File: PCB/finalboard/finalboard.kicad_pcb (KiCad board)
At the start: 4 copper layers, 109.2 x 73.7 mm, 33 parts, among them J1 USB_C_Receptacle_USB2.0, J2 Conn_01x02, J3 Conn_01x04, J6 AudioJack4, Q1 MMDT3904, U1 ESP32-S3-WROOM-1, U3 USBLC6-2SC6, U5 SN74LVC1T45DRL, U6 SN74LVC1T45DRL, U7 AMS1117-3.3, U8 MCP73831-2-OT

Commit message: Incorporated Feedback
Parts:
- removed ?: , 
- removed TP2: TestPoint, TestPoint:TestPoint_Pad_D4.0mm
- added C4: 10u, Capacitor_SMD:C_1206_3216Metric, F.Cu at (82.3, 46.0)
- added C5: 10u, Capacitor_SMD:C_1206_3216Metric, F.Cu at (138.2, 49.5)
- added C6: 0.1u, Capacitor_SMD:C_1206_3216Metric, F.Cu at (92.2, 44.7)
- added D4: GREEN, LED_SMD:LED_1206_3216Metric, B.Cu at (60.7, 32.3)
- added D5: YELLOW, LED_SMD:LED_1206_3216Metric, B.Cu at (85.3, 99.6)
- added D6: 1N5822, Diode_THT:D_DO-201AD_P15.24mm_Horizontal, F.Cu at (89.8, 114.9)
- added D7: BLUE, LED_SMD:LED_1206_3216Metric, F.Cu at (74.7, 111.8)
- added J4: Conn_01x04, Connector_PinHeader_2.54mm:PinHeader_1x04_P2.54mm_Vertical, F.Cu at (32.8, 104.9)
- added J5: Conn_01x02, Connector_PinHeader_2.54mm:PinHeader_1x02_P2.54mm_Vertical, F.Cu at (55.4, 110.9)
- added J7: Conn_01x04, Connector_PinHeader_2.54mm:PinHeader_1x04_P2.54mm_Vertical, F.Cu at (43.9, 106.2)
- added Q3: S8550, Package_TO_SOT_THT:TO-92_Inline, F.Cu at (82.3, 40.1)
- added R10: 10k, Resistor_SMD:R_1206_3216Metric, F.Cu at (125.5, 51.1)
- added R11: 10k, Resistor_SMD:R_1206_3216Metric, F.Cu at (125.5, 54.3)
- added R12: 10k, Resistor_SMD:R_1206_3216Metric, F.Cu at (90.2, 120.0)
- added R13: 100k, Resistor_SMD:R_1206_3216Metric, F.Cu at (90.2, 123.2)
- added R14: R, Resistor_SMD:R_1206_3216Metric, F.Cu at (74.6, 115.2)
- added R15: 6.8k, Resistor_SMD:R_1206_3216Metric, F.Cu at (60.5, 110.2)
- added R16: 10k, Resistor_SMD:R_1206_3216Metric, F.Cu at (60.5, 113.5)
- added R17: 100k, Resistor_SMD:R_1206_3216Metric, F.Cu at (91.9, 49.5)
- added R6: 220, Resistor_SMD:R_1206_3216Metric, F.Cu at (90.4, 40.1)
- added R7: 1000, Resistor_SMD:R_1206_3216Metric, F.Cu at (75.9, 40.9)
- added R8: 4.7k, Resistor_SMD:R_1206_3216Metric, F.Cu at (130.8, 84.8)
- added R9: 470, Resistor_SMD:R_1206_3216Metric, F.Cu at (85.3, 95.2)
- added U10: SN74LVC1T45DRL, Package_TO_SOT_SMD:SOT-563, F.Cu at (121.7, 90.9)
- added U11: MCP23008-xSO, Package_SO:SOIC-18W_7.5x11.6mm_P1.27mm, F.Cu at (80.8, 82.3)
- added U9: SN74LVC1T45DRL, Package_TO_SOT_SMD:SOT-563, F.Cu at (121.7, 87.6)
- D1: value LED -> RED
- D2: value LED -> BLUE
- D3: value LED -> YELLOW
- Q1: value MMDT3904 -> DMG2301L; footprint Package_TO_SOT_SMD:SOT-363_SC-70-6 -> Package_TO_SOT_SMD:SOT-23
- R3, R4, R5: value R -> 470
- moved R5 57.5 mm to (125.2, 42.7)
- moved R3 43.0 mm to (95.2, 53.3)
- moved R4 38.7 mm to (95.2, 56.6)
- moved D3 34.3 mm to (95.2, 32.8)
- moved U8 25.0 mm to (131.1, 89.9)
- moved U7 3.96 mm to (114.0, 82.0)
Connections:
- net Net-(U5-B) renamed /CA_RX
- net Net-(U5-VCCB) renamed /CA_5V
- net Net-(U6-B) renamed /CA_TX
- C1 pad 1: Net-(U3-VBUS) -> Net-(U7-VI)
- D1 pad 1: Net-(D1-K) -> GND
- D1 pad 2: Net-(D1-A) -> /RECORDING_LED
- D2 pad 1: Net-(D2-K) -> GND
- D2 pad 2: Net-(D2-A) -> /WIFI_LED
- D3 pad 1: Net-(D3-K) -> GND
- D3 pad 2: Net-(D3-A) -> /SDCARD_LED
- J1 pad A4: Net-(U3-VBUS) -> /VBUS
- J1 pad A9: Net-(U3-VBUS) -> /VBUS
- J1 pad B4: Net-(U3-VBUS) -> /VBUS
- J1 pad B9: Net-(U3-VBUS) -> /VBUS
- J2 pad 1: unconnected-(J2-Pin_1-Pad1) -> /VBAT
- J2 pad 2: unconnected-(J2-Pin_2-Pad2) -> GND
- J3 pad 1: unconnected-(J3-Pin_1-Pad1) -> /BMS_RX
- J3 pad 2: /ESP_TX2 -> /BMS_TX
- J3 pad 3: /ESP_RX2 -> /BMS_VCC
- Q1 pad 1: Net-(Q1A-E1) -> /VBUS
- Q1 pad 2: /PWR_TRAN_LCD -> Net-(D6-K)
- Q1 pad 3: +3V3 -> /VBAT
- R3 pad 1: GND -> Net-(U4-RXD)
- R3 pad 2: Net-(D1-K) -> /ESP_SS_TX0
- R4 pad 1: GND -> Net-(U4-TX0)
- R4 pad 2: Net-(D2-K) -> /ESP_SS_RX0
- R5 pad 1: GND -> Net-(J4-Pin_2)
- R5 pad 2: Net-(D3-K) -> /ESP_TX0
- U1 pad 12: Net-(D1-A) -> /SDA
- U1 pad 17: Net-(D2-A) -> /SCL
- U1 pad 27: unconnected-(U1-GPIO0/BOOT-Pad27) -> Net-(J5-Pin_2)
- U1 pad 3: unconnected-(U1-EN-Pad3) -> Net-(U1-EN)
- U1 pad 31: Net-(D3-A) -> unconnected-(U1-GPIO38/FSPIWP/SUBSPIWP-Pad31)
- U1 pad 32: unconnected-(U1-MTCK/GPIO39/CLK_OUT3/SUBSPICS1-Pad32) -> Net-(J7-Pin_4)
- U1 pad 33: unconnected-(U1-MTDO/GPIO40/CLK_OUT2-Pad33) -> Net-(J7-Pin_3)
- U1 pad 34: unconnected-(U1-MTDI/GPIO41/CLK_OUT1-Pad34) -> Net-(J7-Pin_2)
- U1 pad 35: unconnected-(U1-MTMS/GPIO42-Pad35) -> Net-(J7-Pin_1)
- U1 pad 38: /PWR_TRAN_TFT -> /LCD_DC
- U1 pad 39: /PWR_TRAN_LCD -> /LED_BACKLIGHT
- U1 pad 4: Net-(U1-GPIO4/TOUCH4/ADC1_CH3) -> /ADC_Battery
- U2 pad 1: Net-(Q1B-E2) -> +3V3
- U2 pad 5: unconnected-(U2-DC/RS-Pad5) -> /LCD_DC
- U2 pad 8: Net-(Q1A-E1) -> /LED_BACKLIGHT
- U3 pad 5: Net-(U3-VBUS) -> /VBUS
- U4 pad 3: /ESP_SS_TX0 -> Net-(U4-RXD)
- U4 pad 4: /ESP_SS_RX0 -> Net-(U4-TX0)
- U4 pad 5: unconnected-(U4-PPS-Pad5) -> Net-(U4-PPS)
- U7 pad 3: Net-(U3-VBUS) -> Net-(U7-VI)
- U8 pad 1: unconnected-(U8-STAT-Pad1) -> Net-(D5-K)
- U8 pad 2: unconnected-(U8-V_{SS}-Pad2) -> GND
- U8 pad 3: unconnected-(U8-V_{BAT}-Pad3) -> /VBAT
- U8 pad 4: unconnected-(U8-V_{DD}-Pad4) -> /VBUS
- U8 pad 5: unconnected-(U8-PROG-Pad5) -> Net-(U8-PROG)
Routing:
- net Net-(J4-Pin_2): track 0.00 -> 18.0 mm, vias 0 -> 1
- net GND: track 22.8 -> 4.70 mm, vias 2 -> 1
- net Net-(D1-K): track 7.97 -> 0.00 mm, vias 1 -> 0
- net /ESP_SS_TX0: track 0.00 -> 7.97 mm
- net Net-(D2-K): track 6.70 -> 0.00 mm, vias 1 -> 0
- net /ADC_Battery: track 0.00 -> 6.70 mm, vias 0 -> 1
- net Net-(U1-EN): track 0.00 -> 5.43 mm, vias 0 -> 1
- net Net-(D3-K): track 5.43 -> 0.00 mm, vias 1 -> 0
- net /VBAT: vias 0 -> 1
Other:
- board text added: "Charging"
- board text added: "GPS"

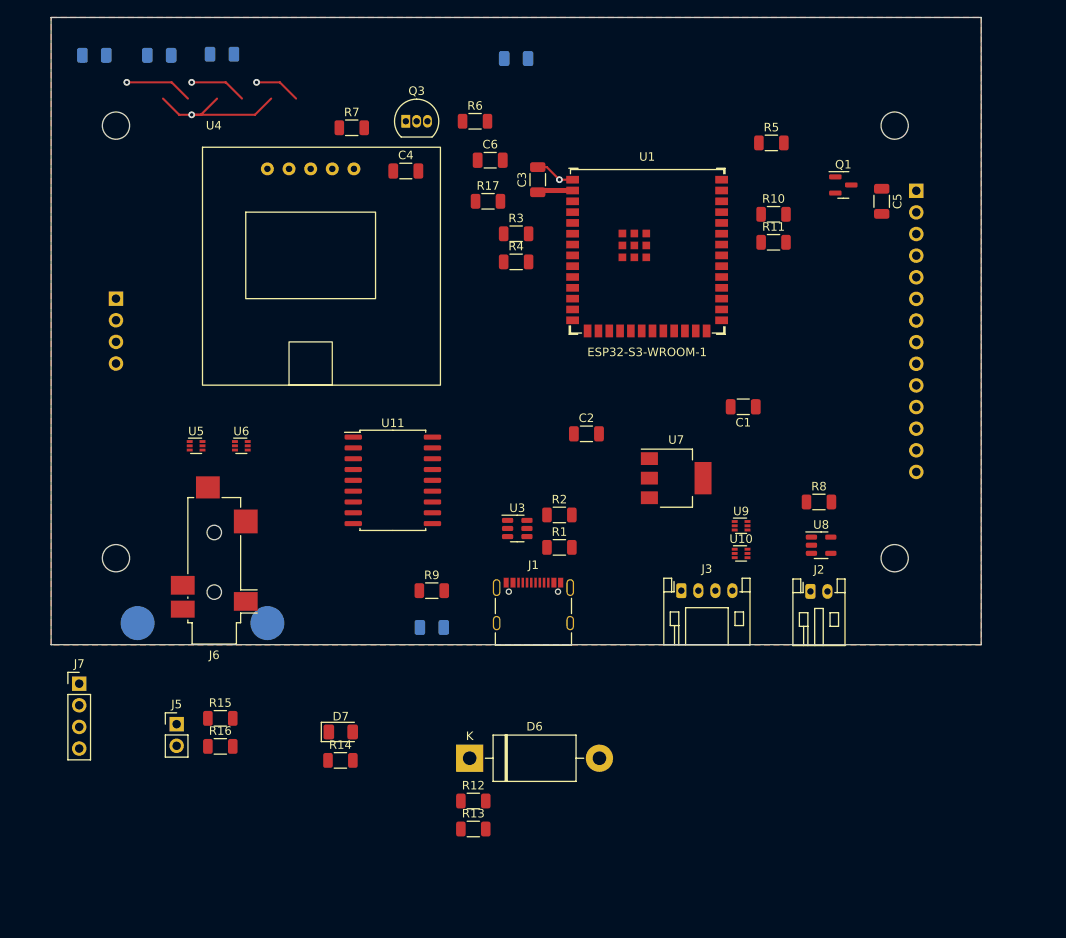
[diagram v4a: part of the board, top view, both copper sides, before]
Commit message: Schematic Mostly Done
check esp32 pins
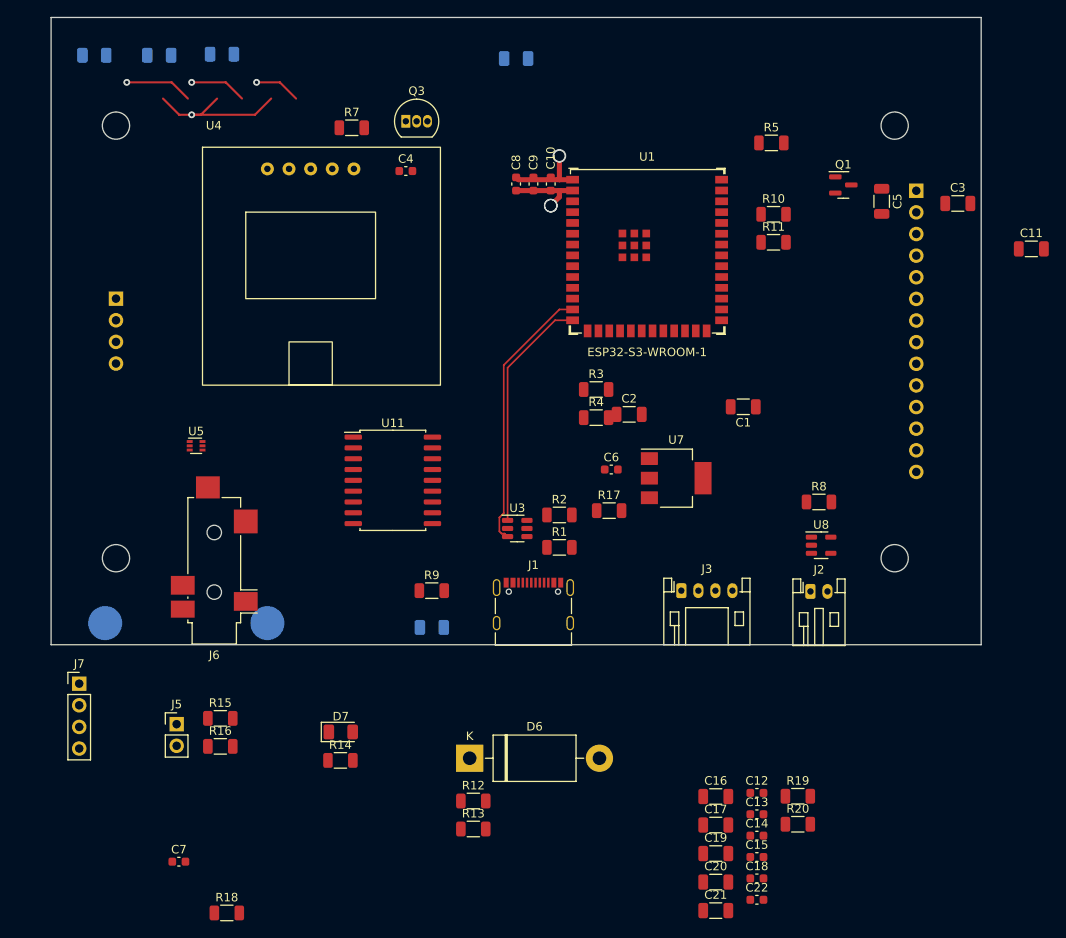
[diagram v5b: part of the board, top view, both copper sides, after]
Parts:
- removed R6: 220, Resistor_SMD:R_1206_3216Metric
- removed TP3: TestPoint, TestPoint:TestPoint_Pad_D4.0mm
- removed U10, U6, U9: SN74LVC1T45DRL, Package_TO_SOT_SMD:SOT-563
- added C10: 0.1u, Capacitor_SMD:C_0603_1608Metric, F.Cu at (99.3, 47.5)
- added C11: 1u, Capacitor_SMD:C_1206_3216Metric, F.Cu at (155.8, 55.1)
- added C12: 0.1u, Capacitor_SMD:C_0603_1608Metric, F.Cu at (123.5, 119.0)
- added C13: 0.1u, Capacitor_SMD:C_0603_1608Metric, F.Cu at (123.5, 121.5)
- added C14: 0.1u, Capacitor_SMD:C_0603_1608Metric, F.Cu at (123.5, 124.0)
- added C15: 0.1u, Capacitor_SMD:C_0603_1608Metric, F.Cu at (123.5, 126.5)
- added C16: 10u, Capacitor_SMD:C_1206_3216Metric, F.Cu at (118.7, 119.4)
- added C17: 10u, Capacitor_SMD:C_1206_3216Metric, F.Cu at (118.7, 122.8)
- added C18: 0.1u, Capacitor_SMD:C_0603_1608Metric, F.Cu at (123.5, 129.0)
- added C19: 0.1u, Capacitor_SMD:C_1206_3216Metric, F.Cu at (118.7, 126.1)
- added C20: 10u, Capacitor_SMD:C_1206_3216Metric, F.Cu at (118.7, 129.5)
- added C21: 10u, Capacitor_SMD:C_1206_3216Metric, F.Cu at (118.7, 132.8)
- added C22: 0.1u, Capacitor_SMD:C_0603_1608Metric, F.Cu at (123.5, 131.6)
- added C7: 1u, Capacitor_SMD:C_0603_1608Metric, F.Cu at (55.6, 127.1)
- added C8: 22u, Capacitor_SMD:C_0603_1608Metric, F.Cu at (95.2, 47.5)
- added C9: 1u, Capacitor_SMD:C_0603_1608Metric, F.Cu at (97.3, 47.5)
- added R18: 100, Resistor_SMD:R_1206_3216Metric, F.Cu at (61.3, 133.1)
- added R19: 470, Resistor_SMD:R_1206_3216Metric, F.Cu at (128.3, 119.4)
- added R20: 470, Resistor_SMD:R_1206_3216Metric, F.Cu at (128.3, 122.7)
- added TP2: TestPoint, TestPoint:TestPoint_Pad_D4.0mm, B.Cu at (47.0, 99.1)
- C1, C2, C5: value 10u -> 22u
- C4, C6: footprint Capacitor_SMD:C_1206_3216Metric -> Capacitor_SMD:C_0603_1608Metric
- R12: value 10k -> 470
- R14: value R -> 470
- R17: value 100k -> 10K
- moved C3 49.4 mm to (147.1, 49.8), turned to 0 degrees
- moved C6 39.0 mm to (106.4, 81.0)
- moved R17 39.0 mm to (106.2, 85.9)
- moved R4 20.6 mm to (104.6, 74.9)
- moved R3 20.6 mm to (104.6, 71.6)
- moved C2 5.51 mm to (108.5, 74.5)
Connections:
- net /SS1 renamed /CS_SD
- net Net-(J5-Pin_2) renamed /BOOT
- net Net-(U7-VI) renamed /Vinput
- D4 pad 2: Net-(D4-A) -> +3V3
- D7 pad 1: Net-(D7-K) -> GND
- J4 pad 4: +3V3 -> /VCC
- R10 pad 2: /SDA -> /SCL
- R11 pad 2: /SCL -> /SDA
- R12 pad 1: Net-(U1-EN) -> Net-(U12-A1)
- R12 pad 2: Net-(R12-Pad2) -> /ESP_TX1
- R14 pad 1: GND -> Net-(U12-A2)
- R14 pad 2: Net-(D7-K) -> /ESP_RX1
- R15 pad 1: /ADC_Battery -> /DIVIDED_VBAT
- R16 pad 2: /ADC_Battery -> /DIVIDED_VBAT
- TP1 pad 1: Net-(U1-GPIO3/TOUCH3/ADC1_CH2) -> Net-(U1-GPIO1/TOUCH1/ADC1_CH0)
- U1 pad 10: /ESP_RX1 -> /ESP_TX1
- U1 pad 11: /ESP_TX2 -> /ESP_RX1
- U1 pad 15: Net-(U1-GPIO3/TOUCH3/ADC1_CH2) -> /DIVIDED_VBAT
- U1 pad 22: /ESP_TX1 -> /CS_LCD
- U1 pad 23: /ESP_RX2 -> /CS_TOUCH
- U1 pad 24: unconnected-(U1-GPIO47/SPICLK_P/SUBSPICLK_P_DIFF-Pad24) -> /LCD_BACKLIGHT
- U1 pad 25: unconnected-(U1-GPIO48/SPICLK_N/SUBSPICLK_N_DIFF-Pad25) -> /LCD_DC
- U1 pad 31: unconnected-(U1-GPIO38/FSPIWP/SUBSPIWP-Pad31) -> /LED_BUILTIN
- U1 pad 38: /LCD_DC -> Net-(U1-GPIO2/TOUCH2/ADC1_CH1)
- U1 pad 39: /LED_BACKLIGHT -> Net-(U1-GPIO1/TOUCH1/ADC1_CH0)
- U1 pad 4: /ADC_Battery -> /ESP_TX2
- U1 pad 5: Net-(U1-GPIO5/TOUCH5/ADC1_CH4) -> /ESP_RX2
- U1 pad 8: unconnected-(U1-GPIO15/U0RTS/ADC2_CH4/XTAL_32K_P-Pad8) -> /LCD_TIRQ
- U2 pad 11: /SS3 -> /CS_TOUCH
- U2 pad 14: unconnected-(U2-T_IRQ-Pad14) -> /LCD_TIRQ
- U2 pad 3: /SS2 -> /CS_LCD
- U2 pad 8: /LED_BACKLIGHT -> /LCD_BACKLIGHT
- U8 pad 1: Net-(D5-K) -> Net-(U8-STAT)
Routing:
- net /USB_D-: track 0.00 -> 31.7 mm
- net /USB_D+: track 0.00 -> 27.9 mm
- net /VBAT: track 0.00 -> 7.97 mm
- net /ESP_SS_TX0: track 7.97 -> 0.00 mm
- net /ESP_TX2: track 0.00 -> 6.70 mm, vias 0 -> 1
- net /ADC_Battery: track 6.70 -> 0.00 mm, vias 1 -> 0
- net GND: track 4.70 -> 9.53 mm
- net +3V3: track 4.17 -> 8.82 mm, vias 0 -> 2
- added copper zone on In2.Cu, net +3V3
- removed copper zone on F.Cu, net +3V3

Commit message: Fixed Footprints, connected all nets
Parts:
- removed C20, C21: 10u, Capacitor_SMD:C_1206_3216Metric
- removed C22: 0.1u, Capacitor_SMD:C_0603_1608Metric
- removed Q3: S8550, Package_TO_SOT_THT:TO-92_Inline
- removed R13: 100k, Resistor_SMD:R_1206_3216Metric
- removed R14, R20: 470, Resistor_SMD:R_1206_3216Metric
- removed R15: 6.8k, Resistor_SMD:R_1206_3216Metric
- removed R16: 10k, Resistor_SMD:R_1206_3216Metric
- removed REF** (x4): MountingHole_3.2mm_M3, MountingHole:MountingHole_3.2mm_M3
- removed U11: MCP23008-xSO, Package_SO:SOIC-18W_7.5x11.6mm_P1.27mm
- added D8: GREEN, LED_SMD:LED_1206_3216Metric, B.Cu at (35.8, 43.4)
- added J8: Conn_01x04, Connector_JST:JST_PH_S4B-PH-K_1x04_P2.00mm_Horizontal, F.Cu at (98.5, 45.9)
- added Q2: S8550, Package_TO_SOT_SMD:SOT-23, F.Cu at (49.1, 50.0)
- added R6: 470, Resistor_SMD:R_1206_3216Metric, F.Cu at (105.7, 81.3)
- added SW1: SW_DIP_x01, Button_Switch_THT:SW_PUSH_6mm_H5mm, B.Cu at (81.8, 41.5)
- added SW2: SW_DIP_x01, Button_Switch_THT:Push_E-Switch_KS01Q01, F.Cu at (82.4, 133.2)
- added U6: PI4ULS5V202, wc_sys_footprint:PI4ULS5V202UEX, F.Cu at (101.8, 52.5)
- added U9: ~, wc_sys_footprint:GT-U7, F.Cu at (46.9, 77.2)
- C1: value 22u -> 0.1u; footprint Capacitor_SMD:C_1206_3216Metric -> Capacitor_SMD:C_0603_1608Metric
- C10, C12, C13: value 0.1u -> 10u; footprint Capacitor_SMD:C_0603_1608Metric -> Capacitor_SMD:C_1206_3216Metric
- C11: value 1u -> 0.1u; footprint Capacitor_SMD:C_1206_3216Metric -> Capacitor_SMD:C_0603_1608Metric
- C16: value 10u -> 0.1u; footprint Capacitor_SMD:C_1206_3216Metric -> Capacitor_SMD:C_0603_1608Metric
- C17: value 10u -> 1u
- C18: value 0.1u -> 22u; footprint Capacitor_SMD:C_0603_1608Metric -> Capacitor_SMD:C_1206_3216Metric
- C19: value 0.1u -> 10u; footprint Capacitor_SMD:C_1206_3216Metric -> Capacitor_SMD:C_0603_1608Metric
- C2: footprint Capacitor_SMD:C_1206_3216Metric -> Capacitor_SMD:C_0603_1608Metric
- C3: value 10u -> 1u; footprint Capacitor_SMD:C_1206_3216Metric -> Capacitor_SMD:C_0603_1608Metric
- C4: value 10u -> 0.1u
- C5: value 22u -> 10u
- C7: value 1u -> 0.1u; footprint Capacitor_SMD:C_0603_1608Metric -> Capacitor_SMD:C_1206_3216Metric
- C8: footprint Capacitor_SMD:C_0603_1608Metric -> Capacitor_SMD:C_1206_3216Metric
- C9: value 1u -> 10u; footprint Capacitor_SMD:C_0603_1608Metric -> Capacitor_SMD:C_1206_3216Metric
- D1: value RED -> 1N5822; footprint LED_SMD:LED_1206_3216Metric -> Diode_SMD:D_SMA; moved to F.Cu
- D2: moved to F.Cu
- D4: value GREEN -> YELLOW
- D5: value YELLOW -> RED
- D6: value 1N5822 -> BLUE; footprint Diode_THT:D_DO-201AD_P15.24mm_Horizontal -> LED_SMD:LED_1206_3216Metric; moved to B.Cu
- D7: value BLUE -> 3.6V; footprint LED_SMD:LED_1206_3216Metric -> Diode_SMD:D_MiniMELF
- J2: value Conn_01x02 -> Conn_01x04; footprint Connector_JST:JST_PH_S2B-PH-K_1x02_P2.00mm_Horizontal -> Connector_PinSocket_2.54mm:PinSocket_1x04_P2.54mm_Vertical
- J3: value Conn_01x04 -> Conn_01x02; footprint Connector_JST:JST_PH_S4B-PH-K_1x04_P2.00mm_Horizontal -> Connector_PinHeader_2.54mm:PinHeader_1x02_P2.54mm_Vertical
- J4: footprint Connector_PinHeader_2.54mm:PinHeader_1x04_P2.54mm_Vertical -> Connector_PinSocket_2.54mm:PinSocket_1x04_P2.54mm_Vertical
- J5: value Conn_01x02 -> Conn_02x06_Counter_Clockwise; footprint Connector_PinHeader_2.54mm:PinHeader_1x02_P2.54mm_Vertical -> Connector_PinSocket_2.54mm:PinSocket_2x06_P2.54mm_Vertical
- J6: value AudioJack4 -> Conn_01x02; footprint Connector_Audio:Jack_3.5mm_CUI_SJ2-3593D-SMT_Horizontal -> Connector_JST:JST_PH_S2B-PH-K_1x02_P2.00mm_Horizontal
- J7: value Conn_01x04 -> AudioJack4; footprint Connector_PinHeader_2.54mm:PinHeader_1x04_P2.54mm_Vertical -> Connector_Audio:Jack_3.5mm_CUI_SJ2-3593D-SMT_Horizontal
- R1: value 5k -> 10K
- R10: value 10k -> 100
- R12: value 470 -> 6.8k
- R17: value 10K -> 470
- R18: value 100 -> 470
- R19: value 470 -> 1k
- R3: value 470 -> 5k
- R4: value 470 -> 100k
- R7: value 1000 -> 10k
- R8: value 4.7k -> 10k
- R9: value 470 -> 4.7k
- U1: value ESP32-S3-WROOM-1 -> USBLC6-2SC6; footprint wc_sys_footprint:ESP32-S3-WROOM-1U -> Package_TO_SOT_SMD:SOT-23-6
- U2: value ~ -> ESP32-S3-WROOM-1; footprint wc_sys_footprint:LCD3.5tft -> wc_sys_footprint:ESP32-S3-WROOM-1U; moved to F.Cu
- U3: value USBLC6-2SC6 -> AMS1117-3.3; footprint Package_TO_SOT_SMD:SOT-23-6 -> Package_TO_SOT_SMD:SOT-223-3_TabPin2
- U4: value ~ -> MCP73831-2-OT; footprint wc_sys_footprint:NEO-6M -> Package_TO_SOT_SMD:SOT-23-5
- U5: value SN74LVC1T45DRL -> MCP23008-xSO; footprint Package_TO_SOT_SMD:SOT-563 -> Package_SO:SOIC-18W_7.5x11.6mm_P1.27mm
- U7: value AMS1117-3.3 -> PI4ULS5V202; footprint Package_TO_SOT_SMD:SOT-223-3_TabPin2 -> wc_sys_footprint:PI4ULS5V202UEX
- U8: value MCP73831-2-OT -> ~; footprint Package_TO_SOT_SMD:SOT-23-5 -> wc_sys_footprint:3.5_inch_SPI_Module_ILI9488; moved to B.Cu
- moved C10 138.5 mm to (234.7, 76.7)
- moved C9 135.5 mm to (229.6, 76.7)
- moved C5 135.4 mm to (270.4, 78.7)
- moved C6 135.4 mm to (238.7, 110.2)
- moved R1 135.4 mm to (232.6, 119.4)
- moved R10 135.4 mm to (257.7, 80.3)
- moved R2 135.4 mm to (232.6, 115.6)
- moved R3 135.4 mm to (236.9, 100.8)
- moved R9 135.4 mm to (217.6, 124.5)
- moved C8 132.3 mm to (224.3, 76.7)
- moved C19 97.8 mm to (44.7, 62.2)
- moved C7 94.9 mm to (150.6, 128.3)
- moved D6 93.2 mm to (30.0, 43.4), turned to 180 degrees
- moved R19 92.4 mm to (56.4, 61.5)
- moved J7 90.8 mm to (113.8, 48.2)
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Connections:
- C1 pad 1: /Vinput -> GND
- C1 pad 2: GND -> Net-(U2-EN)
- C10 pad 1: +3V3 -> +BATT
- C11 pad 1: +3V3 -> GND
- C11 pad 2: GND -> /DIVIDED_VBAT
- C12 pad 1: GND -> /BMS_VCC
- C12 pad 2: /DIVIDED_VBAT -> GND
- C13 pad 1: +3V3 -> /CA_5V
- C14 pad 1: +3V3 -> /BMS_TX
- C15 pad 1: /BMS_TX -> /CA_TX
- C16 pad 1: /CA_5V -> +3V3
- C17 pad 1: /BMS_VCC -> +3V3
- C18 pad 1: /CA_TX -> +3V3
- C5 pad 1: +3V3 -> /Vinput
- C6 pad 2: Net-(U1-EN) -> /Vinput
- C9 pad 1: +3V3 -> VBUS
- D1 pad 1: GND -> Net-(D1-K)
- D1 pad 2: /RECORDING_LED -> VBUS
- D2 pad 2: /WIFI_LED -> /LED_BUILTIN
- D3 pad 1: GND -> Net-(D3-K)
- D3 pad 2: /SDCARD_LED -> VBUS
- D4 pad 1: Net-(D4-K) -> GND
- D4 pad 2: +3V3 -> /SDCARD_LED
- D5 pad 1: Net-(D5-K) -> GND
- D5 pad 2: /VBUS -> /RECORDING_LED
- D6 pad 1: Net-(D6-K) -> GND
- D6 pad 2: /VBUS -> /WIFI_LED
- D7 pad 1: GND -> +3V3
- D7 pad 2: /LED_BUILTIN -> GND
- J1 pad A4: /VBUS -> VBUS
- J1 pad A9: /VBUS -> VBUS
- J1 pad B4: /VBUS -> VBUS
- J1 pad B9: /VBUS -> VBUS
- J2 pad 1: /VBAT -> Net-(J2-Pin_1)
- J2 pad 2: GND -> Net-(J2-Pin_2)
- J3 pad 1: /BMS_RX -> GND
- J3 pad 2: /BMS_TX -> /BOOT
- J4 pad 4: /VCC -> +3V3
- J5 pad 1: GND -> +3V3
- J5 pad 2: /BOOT -> /GPIO35
- Q1 pad 1: /VBUS -> VBUS
- Q1 pad 2: Net-(D6-K) -> Net-(D1-K)
- Q1 pad 3: /VBAT -> +BATT
- R1 pad 1: Net-(J1-CC2) -> +3V3
- R1 pad 2: GND -> Net-(U2-EN)
- R10 pad 1: +3V3 -> Net-(U4-STAT)
- R10 pad 2: /SCL -> Net-(D3-K)
- R11 pad 1: +3V3 -> GND
- R11 pad 2: /SDA -> /DIVIDED_VBAT
- R12 pad 1: Net-(U12-A1) -> /DIVIDED_VBAT
- R12 pad 2: /ESP_TX1 -> +BATT
- R17 pad 1: +3V3 -> Net-(U9-RXD)
- R17 pad 2: Net-(U1-EN) -> /ESP_SS_TX0
- R18 pad 1: Net-(U8-STAT) -> Net-(U9-TXD)
- R18 pad 2: Net-(D5-K) -> /ESP_SS_RX0
- R19 pad 2: /ESP_TX2 -> Net-(U9-PPS)
- R2 pad 1: Net-(J1-CC1) -> Net-(J1-CC2)
- R3 pad 1: Net-(U4-RXD) -> Net-(J1-CC1)
- R3 pad 2: /ESP_SS_TX0 -> GND
- R4 pad 1: Net-(U4-TX0) -> VBUS
- R4 pad 2: /ESP_SS_RX0 -> GND
- R7 pad 1: Net-(Q3-B) -> +3V3
- R7 pad 2: Net-(U4-PPS) -> /SDA
- R8 pad 1: Net-(U8-PROG) -> +3V3
- R8 pad 2: GND -> /SCL
- R9 pad 1: Net-(J4-Pin_3) -> Net-(U4-PROG)
- R9 pad 2: /ESP_RX0 -> GND
- TP1 pad 1: Net-(U1-GPIO1/TOUCH1/ADC1_CH0) -> Net-(U2-GPIO1/TOUCH1/ADC1_CH0)
- TP2 pad 1: Net-(U1-GPIO2/TOUCH2/ADC1_CH1) -> Net-(U2-GPIO2/TOUCH2/ADC1_CH1)
- U1 pad 1: GND -> /USB_D+
- U1 pad 2: +3V3 -> GND
- U1 pad 3: Net-(U1-EN) -> /USB_D-
- U1 pad 4: /ESP_TX2 -> Net-(J1-D--PadA7)
- U1 pad 5: /ESP_RX2 -> VBUS
- U1 pad 6: /ESP_SS_TX0 -> Net-(J1-D+-PadA6)
- U2 pad 1: +3V3 -> GND
- U2 pad 10: /SCK -> /ESP_TX1
- U2 pad 11: /CS_TOUCH -> /ESP_RX1
- U2 pad 12: /MOSI -> /SDA
- U2 pad 13: /MISO -> /USB_D-
- U2 pad 14: /LCD_TIRQ -> /USB_D+
- U2 pad 2: GND -> +3V3
- U2 pad 3: /CS_LCD -> Net-(U2-EN)
- U2 pad 4: unconnected-(U2-RESET-Pad4) -> /ESP_TX2
- U2 pad 5: /LCD_DC -> /ESP_RX2
- U2 pad 6: /MOSI -> /ESP_SS_TX0
- U2 pad 7: /SCK -> /ESP_SS_RX0
- U2 pad 8: /LCD_BACKLIGHT -> /LCD_DC
- U2 pad 9: /MISO -> /LCD_TIRQ
- U3 pad 1: /USB_D+ -> GND
- U3 pad 2: GND -> +3V3
- U3 pad 3: /USB_D- -> /Vinput
- U4 pad 1: +3V3 -> Net-(U4-STAT)
- U4 pad 3: Net-(U4-RXD) -> +BATT
- U4 pad 4: Net-(U4-TX0) -> VBUS
- U4 pad 5: Net-(U4-PPS) -> Net-(U4-PROG)
- U5 pad 1: +3V3 -> /SCL
- U5 pad 2: GND -> /SDA
- U5 pad 3: /ESP_TX1 -> +3V3
- U5 pad 4: /CA_RX -> +3V3
- U5 pad 5: +3V3 -> GND
- U5 pad 6: /CA_5V -> unconnected-(U5-~{RESET}-Pad6)
- U7 pad 1: GND -> +3V3
- U7 pad 2: +3V3 -> /ESP_TX2
- U7 pad 3: /Vinput -> /ESP_RX2
- U8 pad 1: Net-(U8-STAT) -> +3V3
- U8 pad 3: /VBAT -> /CS_LCD
- U8 pad 4: /VBUS -> unconnected-(U8-TFT_RESET-Pad4)
- U8 pad 5: Net-(U8-PROG) -> /LCD_DC
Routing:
- net /USB_D-: track 31.7 -> 0.00 mm
- net /USB_D+: track 27.9 -> 0.00 mm
- net Net-(J4-Pin_2): track 18.0 -> 0.00 mm, vias 1 -> 0
- net GND: track 9.53 -> 0.00 mm, vias 1 -> 0
- net +3V3: track 8.82 -> 0.00 mm, vias 2 -> 0
- net /VBAT: track 7.97 -> 0.00 mm, vias 1 -> 0
- net /ESP_TX2: track 6.70 -> 0.00 mm, vias 1 -> 0
- net Net-(U1-EN): track 5.43 -> 0.00 mm, vias 1 -> 0
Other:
- board size 109.2 x 73.7 mm -> 110 x 70 mm
- board text added: "REC"
- board text added: "SD"
- board text added: "WiFi"
- board text removed: "Recording"
- board text removed: "SDCard"
- board text removed: "WiFi ON"

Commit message: routing initial
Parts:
- C11: footprint Capacitor_SMD:C_0603_1608Metric -> Capacitor_SMD:C_1206_3216Metric
- C16: footprint Capacitor_SMD:C_0603_1608Metric -> Capacitor_SMD:C_0805_2012Metric
- C17: footprint Capacitor_SMD:C_1206_3216Metric -> Capacitor_SMD:C_0805_2012Metric
- C18: value 22u -> 10u; footprint Capacitor_SMD:C_1206_3216Metric -> Capacitor_SMD:C_0805_2012Metric
- C5, C7, C8: footprint Capacitor_SMD:C_1206_3216Metric -> Capacitor_SMD:C_0603_1608Metric
- J7: footprint Connector_Audio:Jack_3.5mm_CUI_SJ2-3593D-SMT_Horizontal -> wc_sys_footprint:SJ-43514-SMT_CUD
- R2, R3: footprint Resistor_SMD:R_1206_3216Metric -> Resistor_SMD:R_0603_1608Metric
- SW2: footprint Button_Switch_THT:Push_E-Switch_KS01Q01 -> Button_Switch_THT:SW_E-Switch_EG2219_DPDT_Angled
- moved C5 178.7 mm to (92.2, 92.7), turned to 90 degrees
- moved R1 175.7 mm to (69.3, 54.4)
- moved R3 164.5 mm to (72.3, 100.1), turned to 180 degrees
- moved R2 153.1 mm to (80.3, 100.1)
- moved C6 145.5 mm to (94.2, 92.7), turned to -90 degrees
- moved R10 144.6 mm to (114.3, 98.6), turned to 180 degrees
- moved C10 128.6 mm to (107.4, 95.2), turned to 0 degrees
- moved C9 125.3 mm to (106.6, 100.6), turned to 0 degrees
- moved C8 119.6 mm to (105.4, 89.7)
- moved R9 112.0 mm to (106.9, 106.9)
- moved C7 57.9 mm to (107.4, 89.7), turned to 90 degrees
- moved SW2 32.5 mm to (86.2, 100.9)
- moved Q1 19.4 mm to (101.4, 100.6)
- moved D4 17.9 mm to (23.9, 43.4)
- moved R7 17.6 mm to (69.8, 73.9)
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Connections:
- net Net-(J1-D+-PadA6) renamed /D_P
- net Net-(J1-D--PadA7) renamed /D_N
- SW2 pad 1: Net-(D1-K) -> /Vinput
- SW2 pad 2: /Vinput -> Net-(D1-K)
- SW2 pad 3: (no net) -> unconnected-(SW2-C-Pad3)
- SW2 pad 4: (no net) -> /Vinput
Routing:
- net /SCK: track 0.00 -> 116.7 mm, vias 0 -> 2
- net /MOSI: track 0.00 -> 116.6 mm, vias 0 -> 2
- net /MISO: track 0.00 -> 111.7 mm, vias 0 -> 4
- net GND: track 0.00 -> 86.2 mm, vias 0 -> 27
- net /LCD_TIRQ: track 0.00 -> 79.1 mm, vias 0 -> 2
- net /SCL: track 0.00 -> 71.8 mm, vias 0 -> 4
- net /CS_SD: track 0.00 -> 57.2 mm, vias 0 -> 3
- net /SDA: track 0.00 -> 53.2 mm, vias 0 -> 2
- net +3V3: track 0.00 -> 52.5 mm, vias 0 -> 9
- net /CS_TOUCH: track 0.00 -> 50.6 mm, vias 0 -> 2
- net +BATT: track 0.00 -> 50.2 mm
- net /CS_LCD: track 0.00 -> 46.8 mm
- net /SDCARD_LED: track 0.00 -> 29.6 mm, vias 0 -> 1
- net Net-(D3-K): track 0.00 -> 26.1 mm, vias 0 -> 1
- net Net-(D1-K): track 0.00 -> 25.6 mm, vias 0 -> 2
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- added copper zone on F.Cu, net GND
- added copper zone on B.Cu, net VBUS
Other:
- board text added: "Charge"
- board text added: "Rev 1.0 Genesis"
- board text removed: "Charging"
